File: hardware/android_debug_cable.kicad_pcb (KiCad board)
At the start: 2 copper layers, 25.5 x 10.5 mm, 11 parts, among them P1 USB_OTG, P2 50-00397, P3 CONN_01X04, U1 TCR2EF18, U2 CP2102N-A01-GQFN24

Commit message: v0.6
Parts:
- turned C1 to 180 degrees
- renumbered G*** to LOGO
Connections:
- C1 pad 1: Net-(C1-Pad1) -> V3.3
- C1 pad 2: V3.3 -> GND
- U2 pad 6: Net-(C1-Pad1) -> V3.3
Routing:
- net V3.3: track 46.4 -> 56.1 mm, vias 2 -> 3
- net Net-(C1-Pad1): track 8.29 -> 0.00 mm, vias 2 -> 0
- net GND: track 94.1 -> 96.0 mm
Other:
- board text added: "v0.6"
- board text removed: "v0.5"

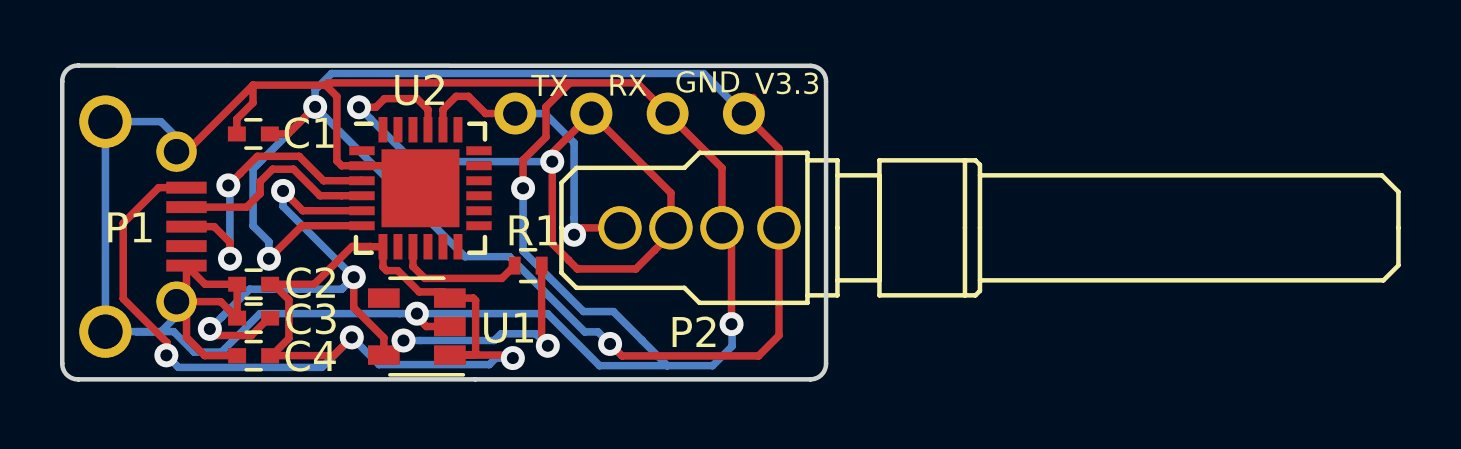
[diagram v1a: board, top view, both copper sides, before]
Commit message: Fixed VBUS not being connected, shrunk connector through holes
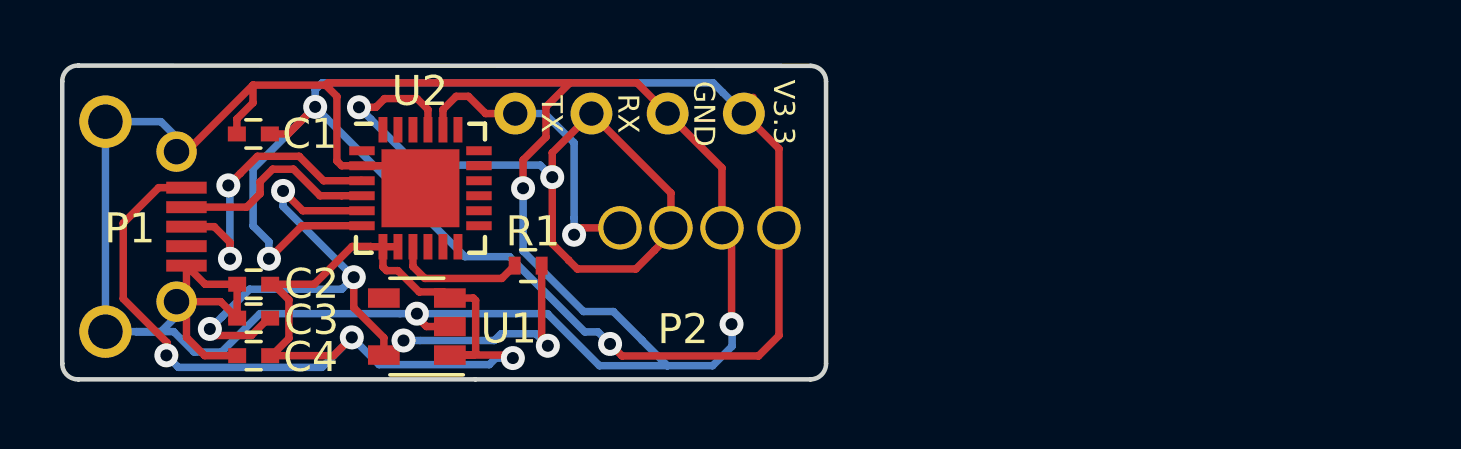
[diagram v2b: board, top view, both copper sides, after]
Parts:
- removed LOGO: LOGO, memcpy_logo:memcpy_logo_13.2x3.6mm
- added W1: LOGO, copperhead_logo:copperhead_logo, B.Cu at (141.4, 88.4)
- P2: footprint 54-00035:54-00035 -> 54-00035:54-00035_nosilk
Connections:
- P1 pad 4: (no net) -> Net-(P1-Pad4)
- U1 pad 4: (no net) -> Net-(U1-Pad4)
- U2 pad 1: (no net) -> Net-(U2-Pad1)
- U2 pad 10: (no net) -> Net-(U2-Pad10)
- U2 pad 11: (no net) -> Net-(U2-Pad11)
- U2 pad 12: (no net) -> Net-(U2-Pad12)
- U2 pad 13: (no net) -> Net-(U2-Pad13)
- U2 pad 14: (no net) -> Net-(U2-Pad14)
- U2 pad 15: (no net) -> Net-(U2-Pad15)
- U2 pad 16: (no net) -> Net-(U2-Pad16)
- U2 pad 17: (no net) -> Net-(U2-Pad17)
- U2 pad 18: (no net) -> Net-(U2-Pad18)
- U2 pad 19: (no net) -> Net-(U2-Pad19)
- U2 pad 22: (no net) -> Net-(U2-Pad22)
- U2 pad 23: (no net) -> Net-(U2-Pad23)
- U2 pad 24: (no net) -> Net-(U2-Pad24)
- U2 pad 8: (no net) -> VCC
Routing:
- net VCC: track 39.8 -> 40.3 mm

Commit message: v0.7
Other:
- board text added: "v0.7"
- board text removed: "v0.6"
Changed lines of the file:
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@@
   (general
     (thickness 1.6)
-    (drawings 14)
+    (drawings 18)
     (tracks 251)
     (zones 0)
@@
       (xy 0.286595 4.997953)) (layer B.SilkS) (width 0.01))
   )
+  (gr_text TX (at 147.59 86.35 180) (layer B.SilkS)
+    (effects (font (size 0.7 0.7) (thickness 0.15)) (justify mirror))
+  )
+  (gr_text RX (at 150.13 86.35 180) (layer B.SilkS)
+    (effects (font (size 0.7 0.7) (thickness 0.15)) (justify mirror))
+  )
+  (gr_text GND (at 152.64 86.35 180) (layer B.SilkS)
+    (effects (font (size 0.7 0.7) (thickness 0.15)) (justify mirror))
+  )
+  (gr_text V3.3 (at 155.21 86.35 180) (layer B.SilkS)
+    (effects (font (size 0.7 0.7) (thickness 0.15)) (justify mirror))
+  )
   (gr_text V3.3 (at 156.51 84.83 270) (layer F.SilkS)
     (effects (font (size 0.7 0.7) (thickness 0.15)))
@@
     (effects (font (size 0.7 0.7) (thickness 0.15)))
   )
-  (gr_text v0.6 (at 147.94 88.71 180) (layer B.SilkS)
+  (gr_text v0.7 (at 147.94 88.71 180) (layer B.SilkS)
     (effects (font (size 0.7 0.7) (thickness 0.15)) (justify mirror))
   )
